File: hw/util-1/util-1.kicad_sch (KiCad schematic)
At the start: 0 parts

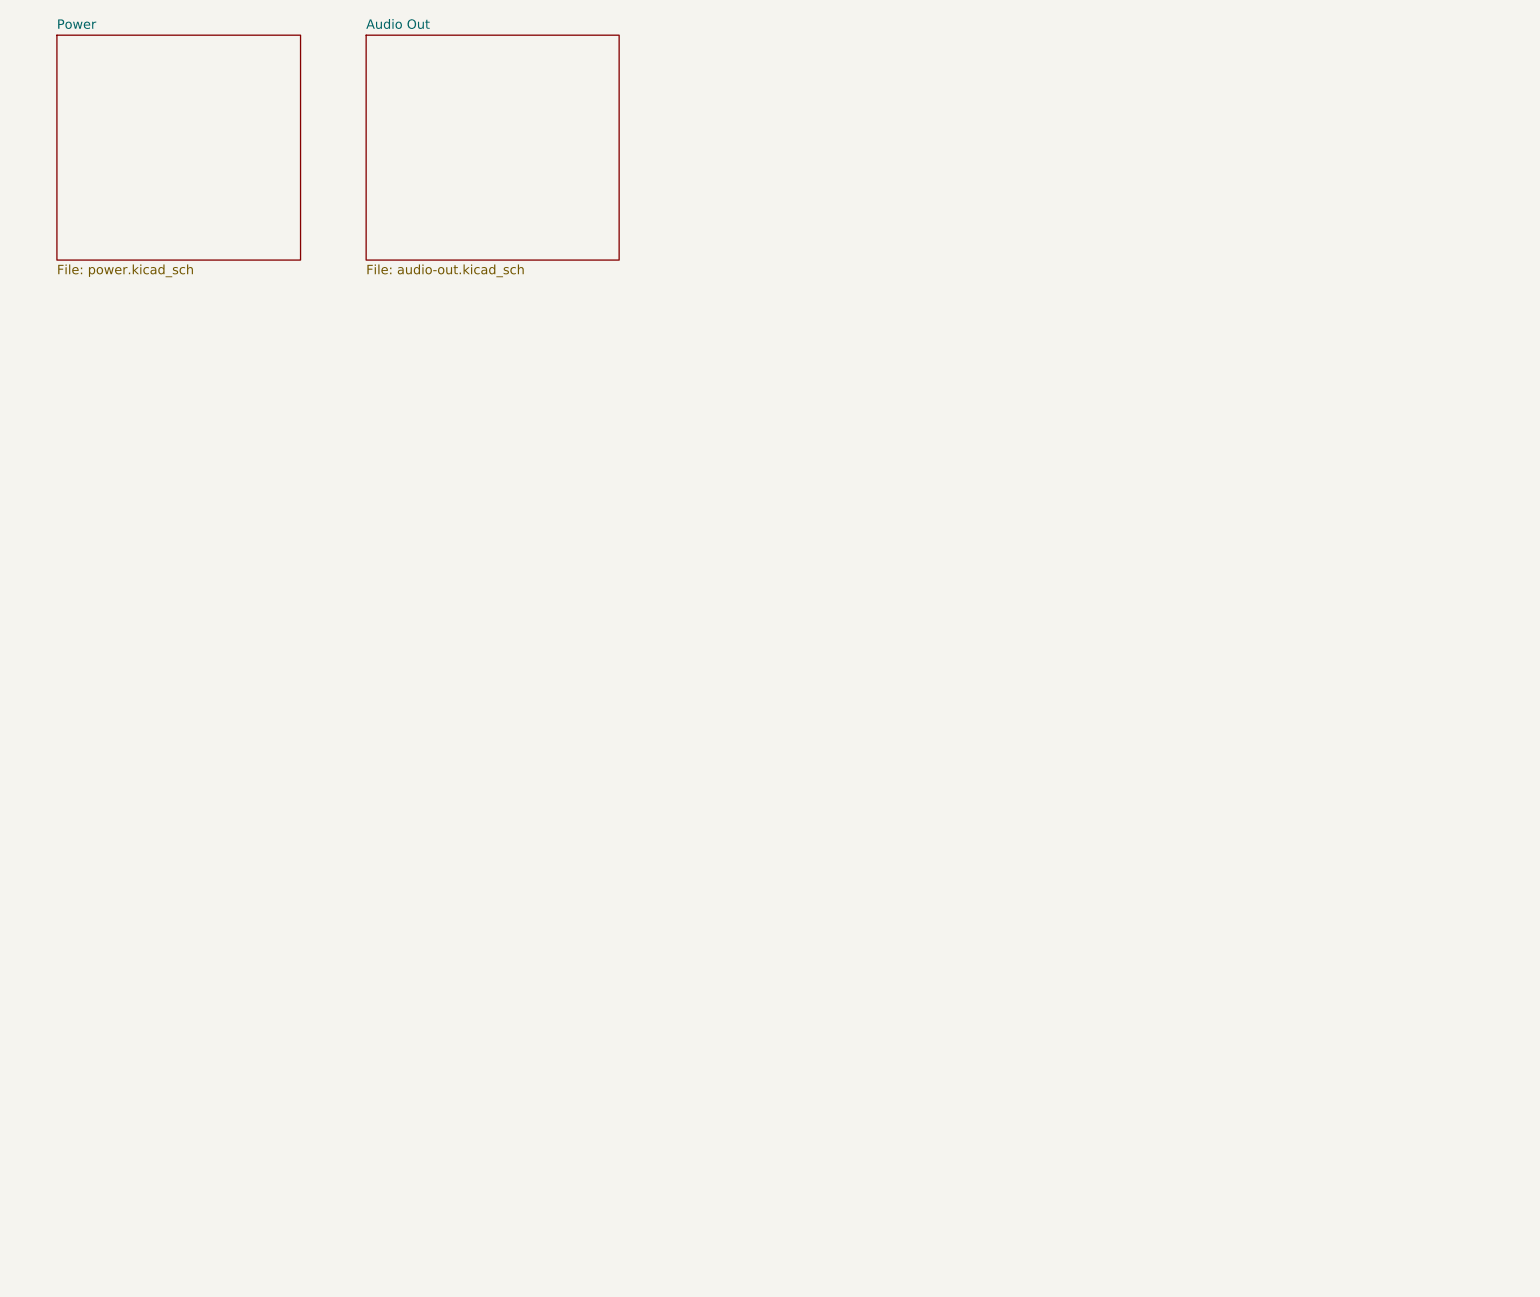
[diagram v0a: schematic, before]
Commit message: Initial version of PCB layout
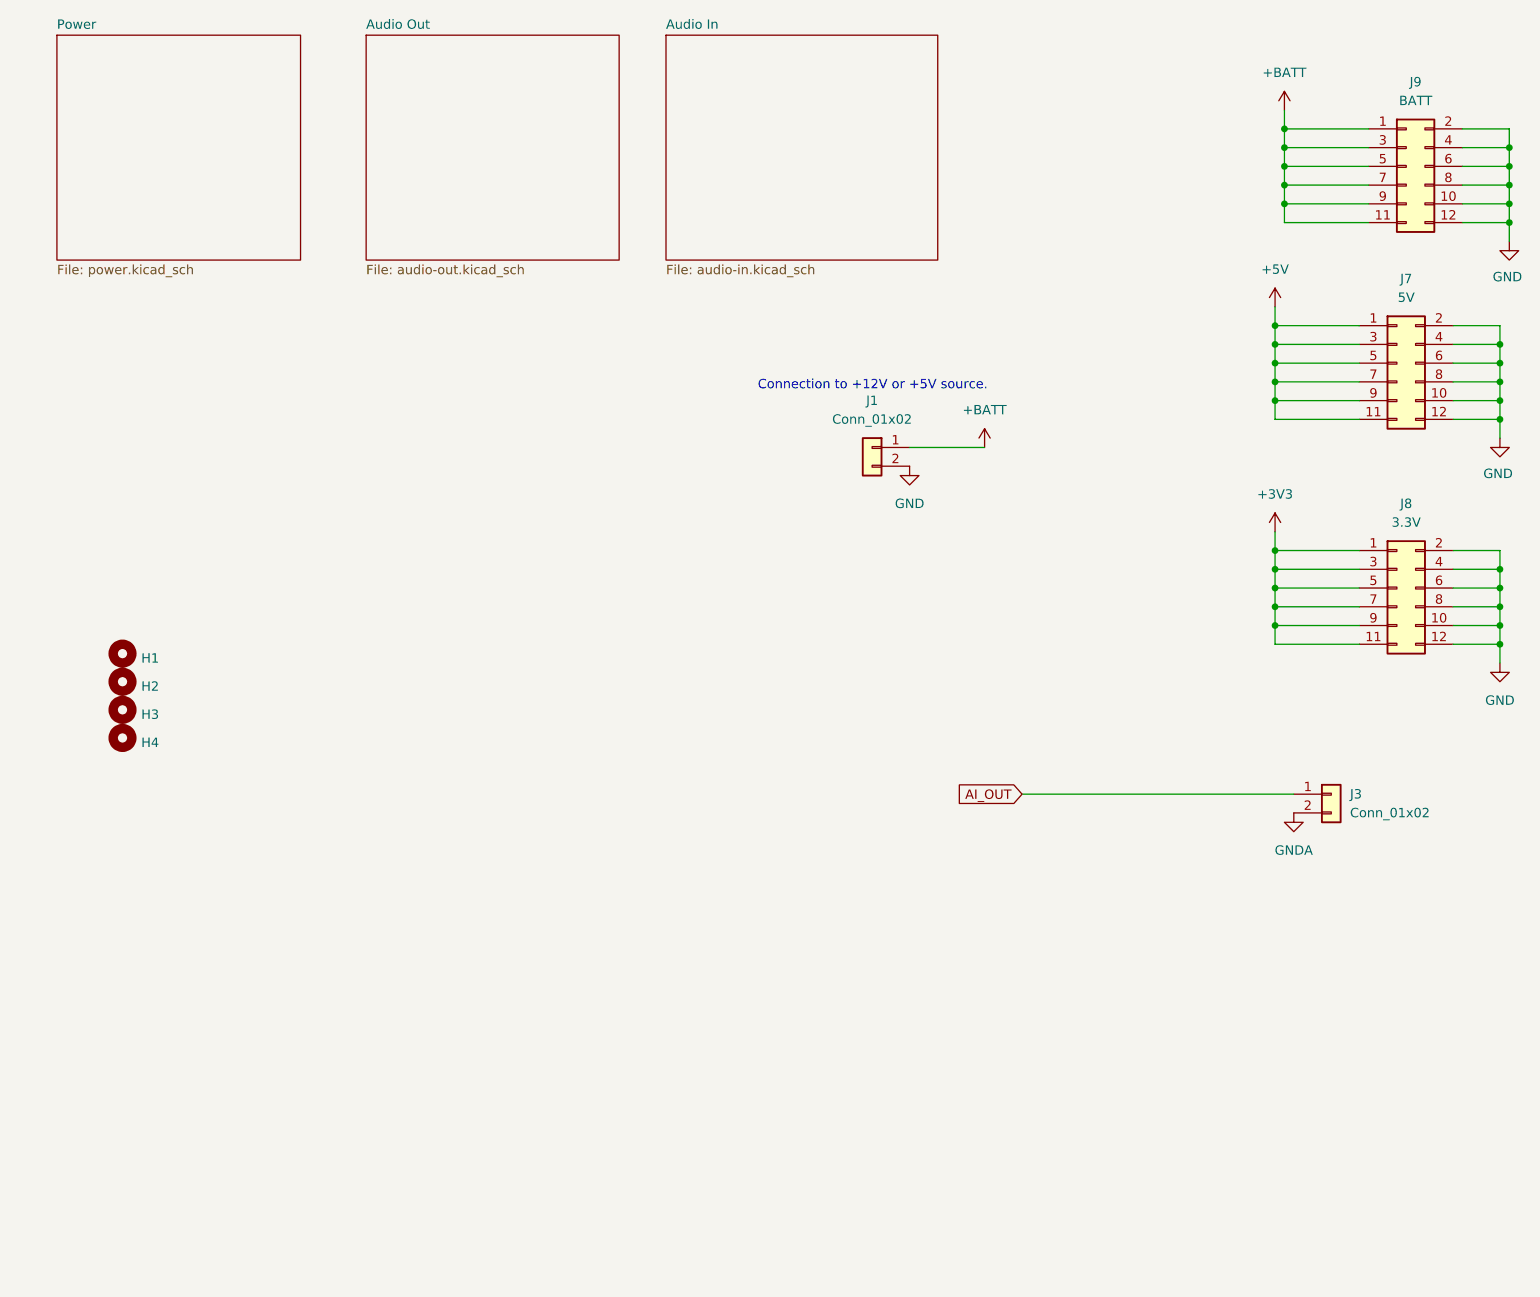
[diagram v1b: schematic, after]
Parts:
- added H1, H2, H3, H4: MountingHole, MountingHole:MountingHole_4mm, symbol Mechanical:MountingHole
- added J1, J3: Conn_01x02, Connector_PinHeader_2.54mm:PinHeader_1x02_P2.54mm_Vertical, symbol Connector_Generic:Conn_01x02
- added J7: 5V, Connector_PinHeader_2.54mm:PinHeader_2x06_P2.54mm_Vertical, symbol Connector_Generic:Conn_02x06_Odd_Even
- added J8: 3.3V, Connector_PinHeader_2.54mm:PinHeader_2x06_P2.54mm_Vertical, symbol Connector_Generic:Conn_02x06_Odd_Even
- added J9: BATT, Connector_PinHeader_2.54mm:PinHeader_2x06_P2.54mm_Vertical, symbol Connector_Generic:Conn_02x06_Odd_Even
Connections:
- new net +3V3: J8.1 (Pin_1), J8.11 (Pin_11), J8.3 (Pin_3), J8.5 (Pin_5), J8.7 (Pin_7), J8.9 (Pin_9)
- new net +5V: J7.1 (Pin_1), J7.11 (Pin_11), J7.3 (Pin_3), J7.5 (Pin_5), J7.7 (Pin_7), J7.9 (Pin_9)
- new net +BATT: J1.1 (Pin_1), J9.1 (Pin_1), J9.11 (Pin_11), J9.3 (Pin_3), J9.5 (Pin_5), J9.7 (Pin_7), J9.9 (Pin_9)
- new net AI_OUT: J3.1 (Pin_1)
- new net GND: J1.2 (Pin_2), J7.10 (Pin_10), J7.12 (Pin_12), J7.2 (Pin_2), J7.4 (Pin_4), J7.6 (Pin_6), J7.8 (Pin_8), J8.10 (Pin_10), J8.12 (Pin_12), J8.2 (Pin_2), J8.4 (Pin_4), J8.6 (Pin_6), J8.8 (Pin_8), J9.10 (Pin_10), J9.12 (Pin_12), J9.2 (Pin_2), J9.4 (Pin_4), J9.6 (Pin_6), J9.8 (Pin_8)
- new net GNDA: J3.2 (Pin_2)
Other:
- added sheet Audio In (audio-in.kicad_sch)
- note added: "Connection to +12V or +5V source."
- company: (none) -> Bruce MacKinnon KC1FSZ
- title: (none) -> Utility Board 1

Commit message: Ready to sent to fab
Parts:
- added C13: 0.1uF, Capacitor_SMD:C_0805_2012Metric_Pad1.18x1.45mm_HandSolder, symbol Device:C_Small
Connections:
- net +BATT: now also C13.1
- net GND: now also C13.2
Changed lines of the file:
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@@
+	)
+	(junction
+		(at 151.13 78.74)
+		(diameter 0)
+		(color 0 0 0 0)
 	)
 	(junction
@@
 	(wire
 		(pts
+			(xy 151.13 78.74) (xy 153.67 78.74)
+		)
+		(stroke
+			(width 0)
+			(type default)
+		)
+	)
+	(wire
+		(pts
 			(xy 218.44 43.18) (xy 224.79 43.18)
 		)
@@
 	(wire
 		(pts
-			(xy 143.51 78.74) (xy 153.67 78.74)
+			(xy 143.51 78.74) (xy 151.13 78.74)
 		)
 		(stroke
@@
 				(justify right)
 				(hide yes)
+			)
+		)
+	)
+	(symbol
+		(lib_id "Device:C_Small")
+		(at 151.13 81.28 0)
+		(unit 1)
+		(exclude_from_sim no)
+		(in_bom yes)
+		(on_board yes)
+		(dnp no)
+		(fields_autoplaced yes)
+		(property "Reference" "C13"
+			(at 153.67 80.0162 0)
+			(effects
+				(font
+					(size 1.27 1.27)
+				)
+				(justify left)
+			)
+		)
+		(property "Value" "0.1uF"
+			(at 153.67 82.5562 0)
+			(effects
+				(font
+					(size 1.27 1.27)
+				)
+				(justify left)
+			)
+		)
+		(property "Footprint" "Capacitor_SMD:C_0805_2012Metric_Pad1.18x1.45mm_HandSolder"
+			(at 151.13 81.28 0)
+			(effects
+				(font
+					(size 1.27 1.27)
+				)
+				(hide yes)
+			)
+		)
+		(property "Datasheet" "~"
+			(at 151.13 81.28 0)
+			(effects
+				(font
+					(size 1.27 1.27)
+				)
+				(hide yes)
+			)
+		)
+		(property "Description" "Unpolarized capacitor, small symbol"
+			(at 151.13 81.28 0)
+			(effects
+				(font
+					(size 1.27 1.27)
+				)
+				(hide yes)
+			)
+		)
+		(pin "2"
+		)
+		(pin "1"
+		)
+		(instances
+			(project ""
+				(path "/79e94c33-63da-4751-adae-72fc4eafefd8"
+					(reference "C13")
+					(unit 1)
+				)
 			)
 		)
@@
 					(unit 1)
 				)
+			)
+		)
+	)
+	(symbol
+		(lib_id "power:GND")
+		(at 151.13 83.82 0)
+		(unit 1)
+		(exclude_from_sim no)
+		(in_bom yes)
+		(on_board yes)
+		(dnp no)
+		(fields_autoplaced yes)
+		(property "Reference" "#PWR033"
+			(at 151.13 90.17 0)
+			(effects
+				(font
+					(size 1.27 1.27)
+				)
+				(hide yes)
+			)
+		)
+		(property "Value" "GND"
+			(at 151.13 88.9 0)
+			(effects
+				(font
+					(size 1.27 1.27)
+				)
+			)
+		)
+		(property "Footprint" ""
+			(at 151.13 83.82 0)
+			(effects
+				(font
+					(size 1.27 1.27)
+				)
+				(hide yes)
+			)
+		)
+		(property "Datasheet" ""
+			(at 151.13 83.82 0)
+			(effects
+				(font
+					(size 1.27 1.27)
+				)
+				(hide yes)
+			)
+		)
+		(property "Description" "Power symbol creates a global label with name \"GND\" , ground"
+			(at 151.13 83.82 0)
+			(effects
+				(font
+					(size 1.27 1.27)
+				)
+				(hide yes)
+			)
+		)
+		(pin "1"
+		)
+		(instances
+			(project "util-1"
+				(path "/79e94c33-63da-4751-adae-72fc4eafefd8"
+					(reference "#PWR033")
+					(unit 1)
+				)

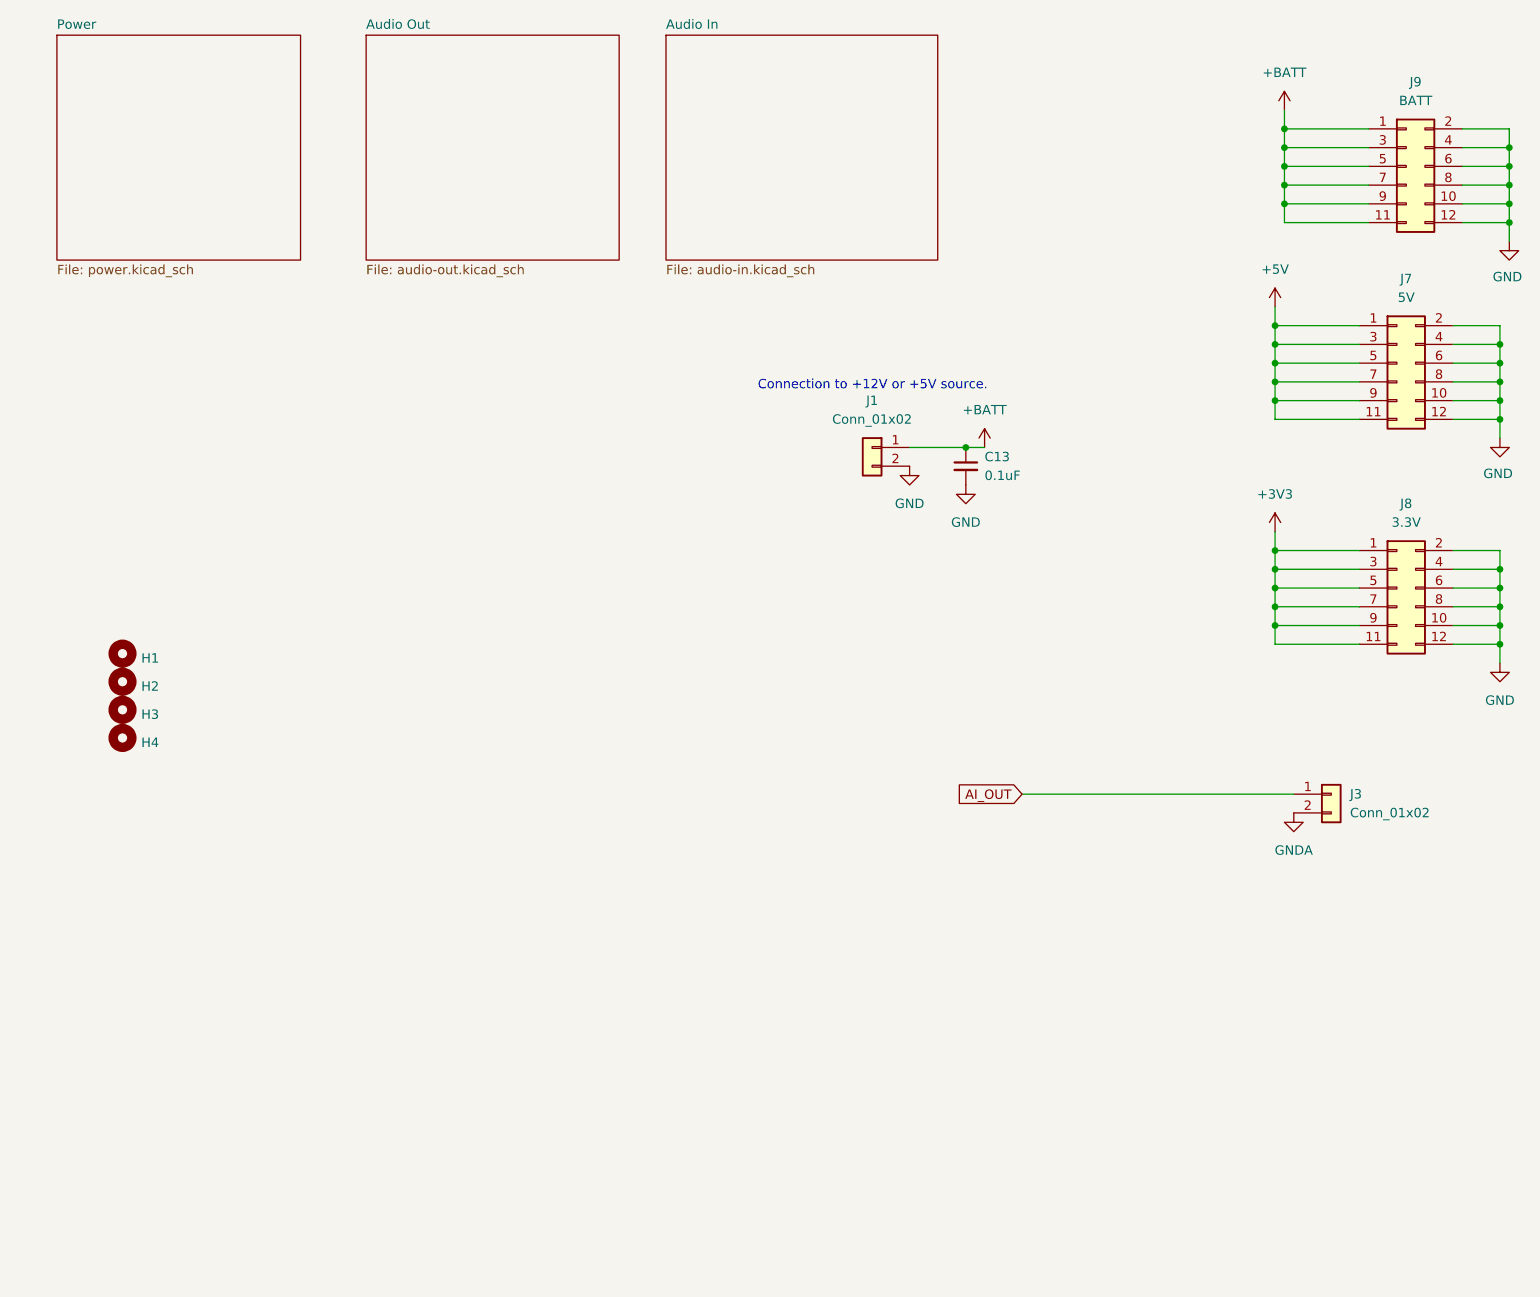
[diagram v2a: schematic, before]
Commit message: Sending revision of util-1 to JLCPCB
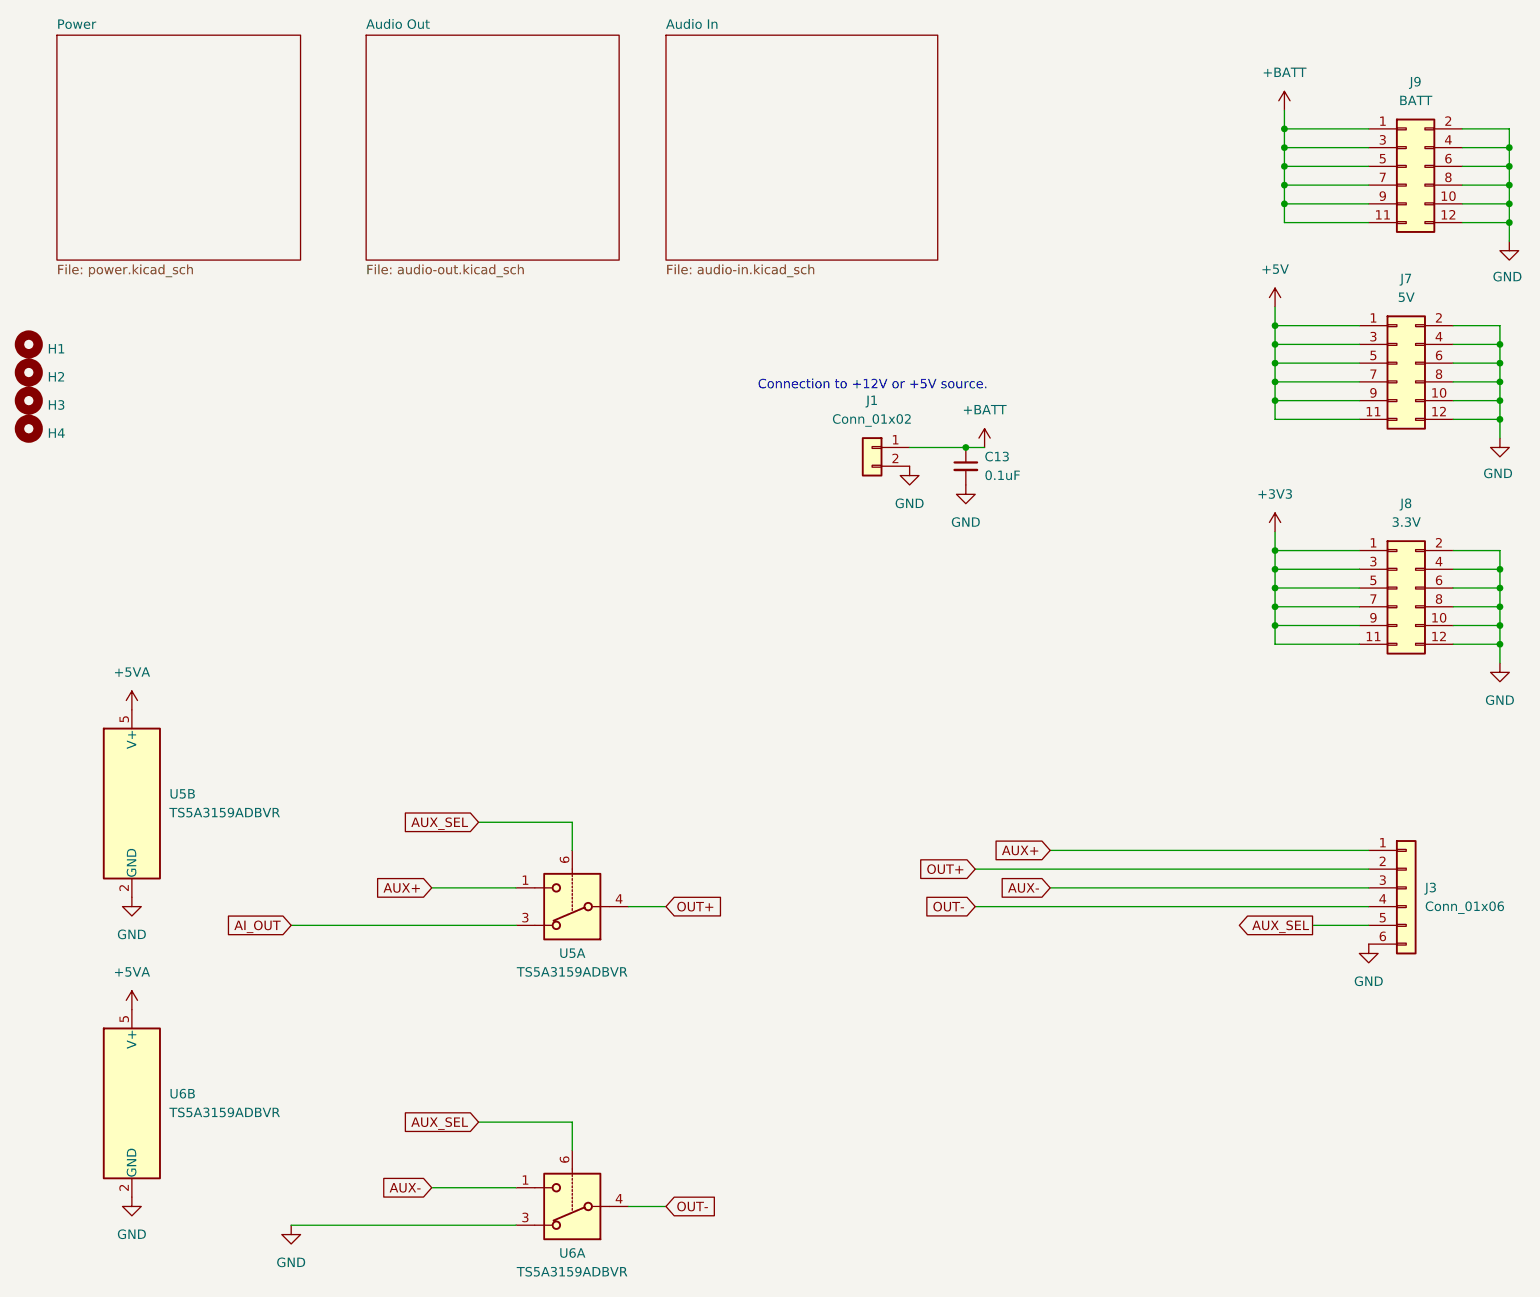
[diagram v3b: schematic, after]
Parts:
- removed J3: Conn_01x02, Connector_PinHeader_2.54mm:PinHeader_1x02_P2.54mm_Vertical, symbol Connector_Generic:Conn_01x02
- added J3: Conn_01x06, Connector_PinHeader_2.54mm:PinHeader_1x06_P2.54mm_Vertical, symbol Connector_Generic:Conn_01x06
- added U5, U6: TS5A3159ADBVR, Package_TO_SOT_SMD:SOT-23-6, symbol Analog_Switch:TS5A3159ADBVR
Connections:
- net AI_OUT: now also U5.3
- net GND: now also J3.6 (Pin_6), U5.2 (GND), U6.2 (GND), U6.3
- new net +5VA: U5.5 (V+), U6.5 (V+)
- new net AUX+: J3.1 (Pin_1), U5.1
- new net AUX-: J3.3 (Pin_3), U6.1
- new net AUX_SEL: J3.5 (Pin_5), U5.6, U6.6
- new net OUT+: J3.2 (Pin_2), U5.4
- new net OUT-: J3.4 (Pin_4), U6.4
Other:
- moved on the sheet: H1, H2, H3, H4
